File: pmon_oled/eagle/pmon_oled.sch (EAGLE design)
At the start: 37 parts, among them J1 USB, J2 USB, J4 PINHD-1X3, J5 PINHD-2X3, Q1 16Mhz, U1 LTC2943, U2 FT232RL, U3 LT1764AEQ, U4 ATMEGA328TQFP32

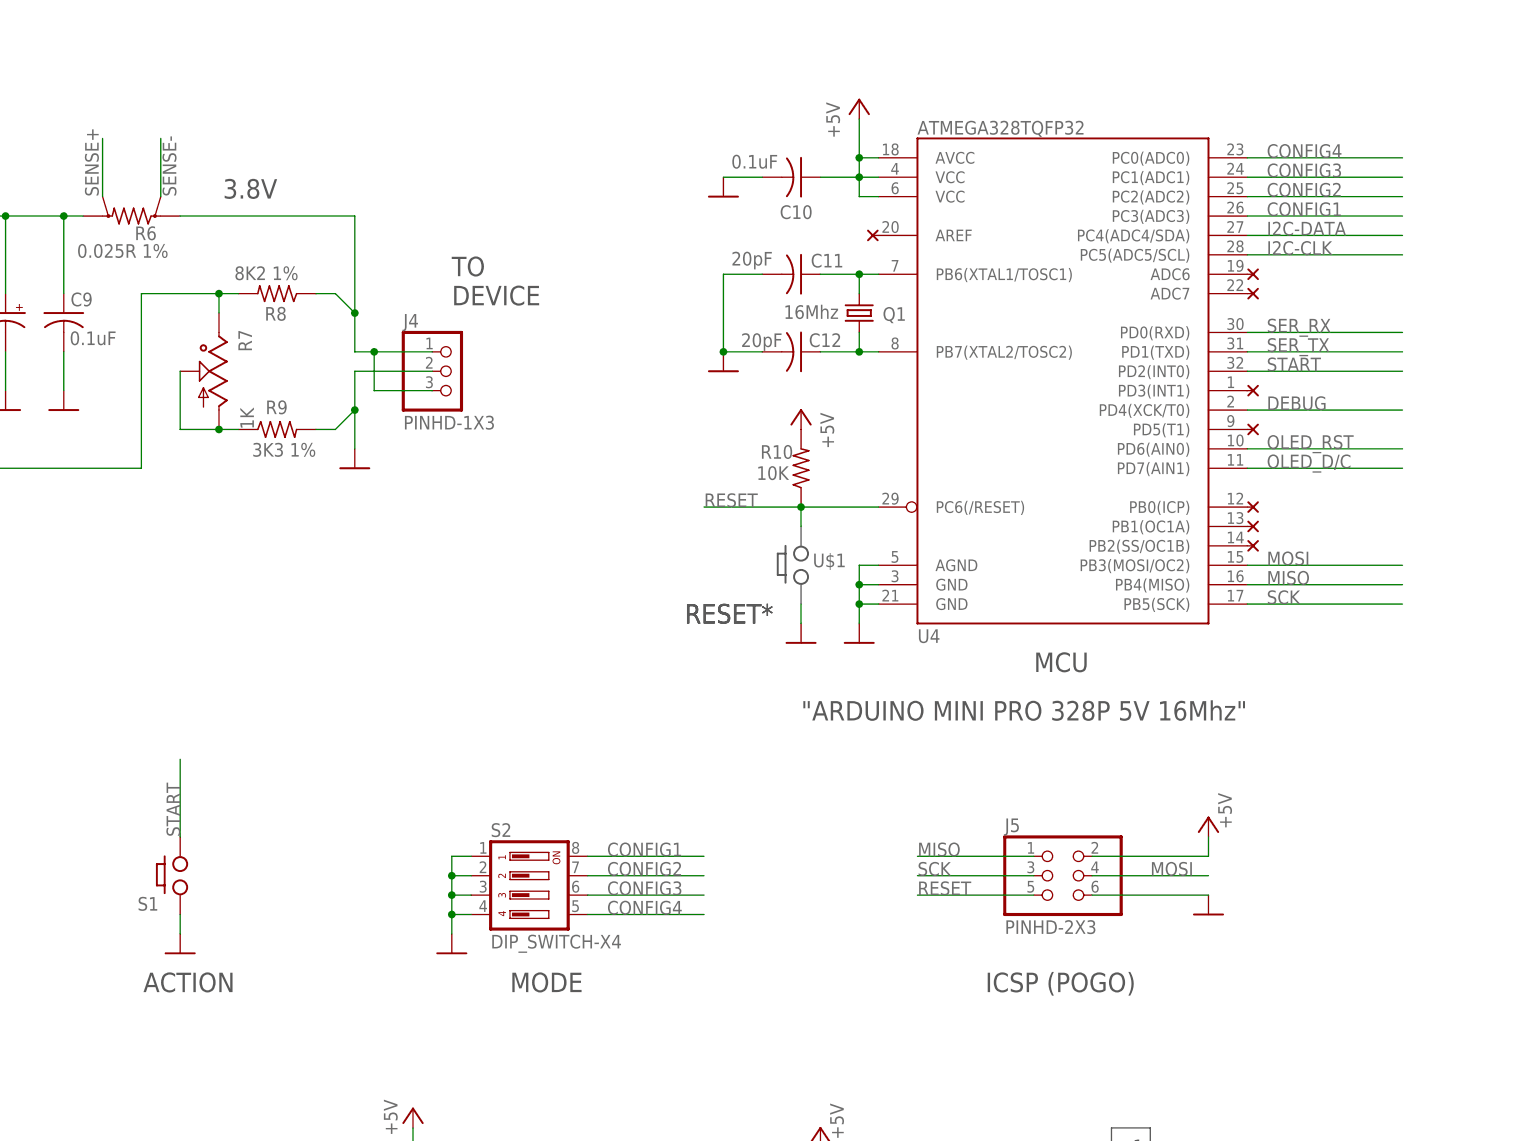
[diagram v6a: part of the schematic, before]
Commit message: Removed the config dip switches.
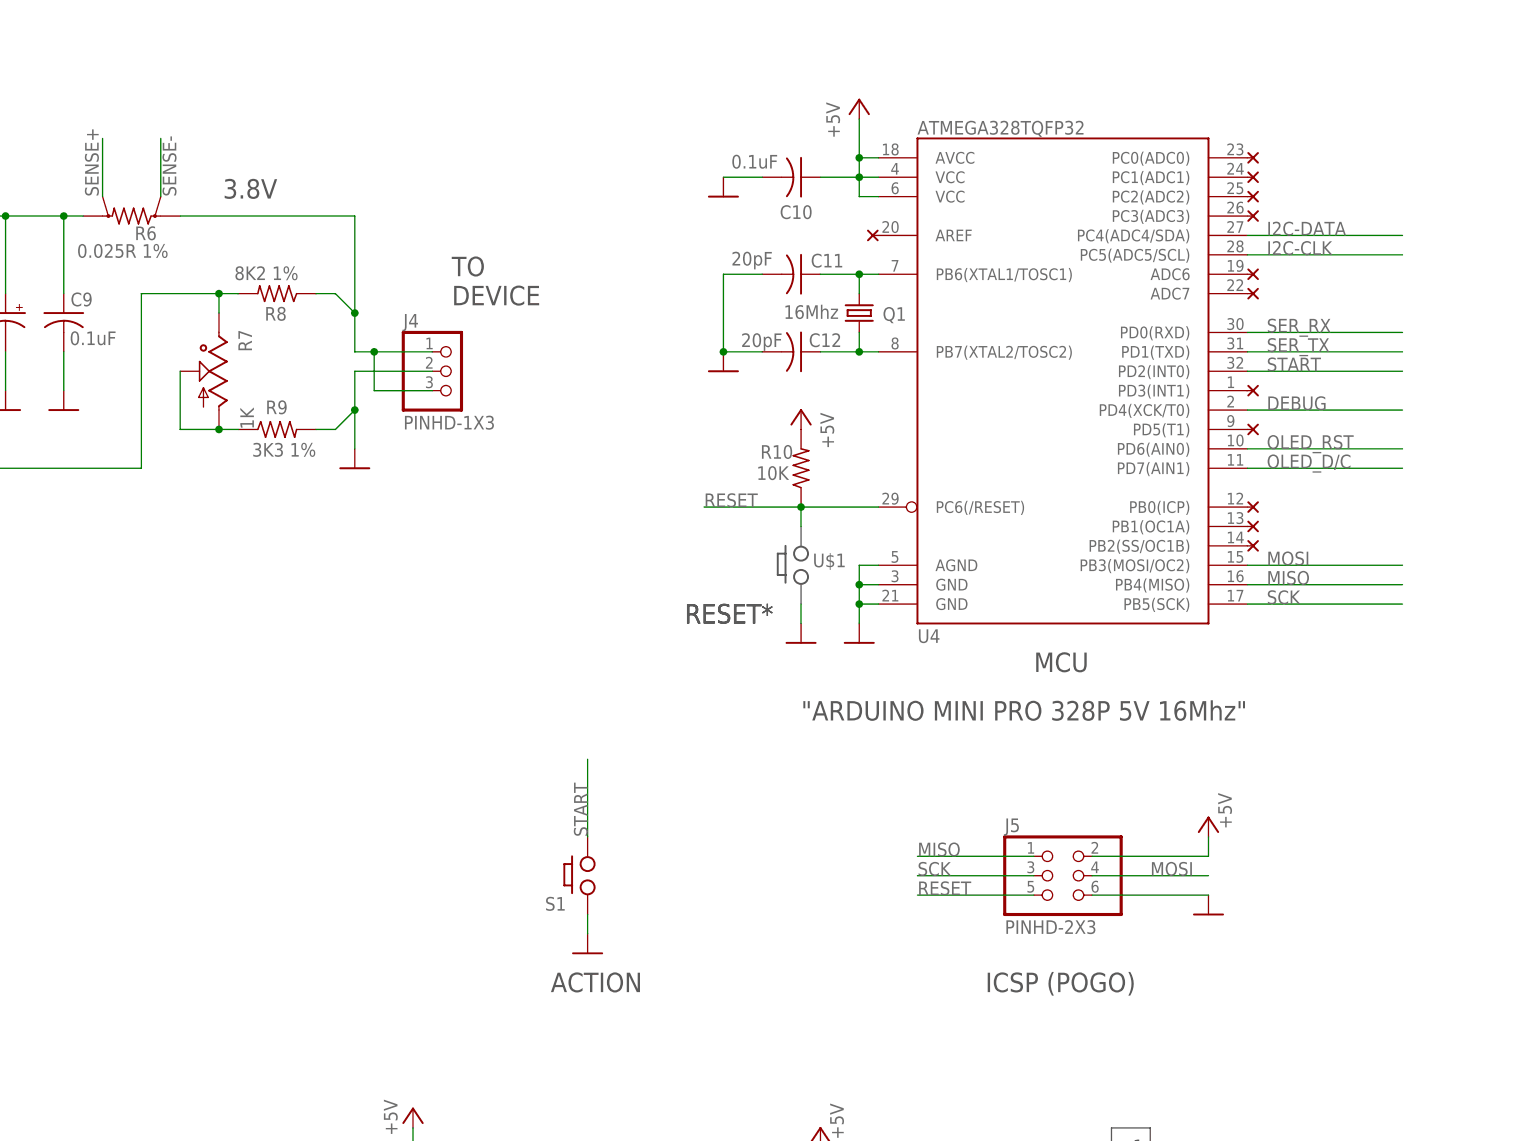
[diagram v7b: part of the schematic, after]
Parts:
- removed S2: DIP_SWITCH-X4, pmon_oled:DIP_SWITCH-X4
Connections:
- removed net CONFIG1: S2.8, U4.PC3(ADC3)
- removed net CONFIG2: S2.7, U4.PC2(ADC2)
- removed net CONFIG3: S2.6, U4.PC1(ADC1)
- removed net CONFIG4: S2.5, U4.PC0(ADC0)
- net GND: no longer S2.1, S2.2, S2.3, S2.4
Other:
- note removed: "MODE"
- moved on the sheet: S1
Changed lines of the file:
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@@
 <part name="P+12" library="pmon_oled" deviceset="+5V" device=""/>
 <part name="GND29" library="pmon_oled" deviceset="GND" device=""/>
-<part name="S2" library="pmon_oled" deviceset="DIP_SWITCH-X4" device=""/>
-<part name="GND30" library="pmon_oled" deviceset="GND" device=""/>
 <part name="J1" library="pmon_oled" deviceset="USB" device=""/>
 <part name="R7" library="pmon_oled" deviceset="TRIM_US-" device="SM-42/43A" value="1K"/>
@@
 <part name="U$14" library="pmon_oled" deviceset="NC" device=""/>
 <part name="S1" library="pmon_oled" deviceset="PUSH_BUTTON" device=""/>
+<part name="U$15" library="pmon_oled" deviceset="NC" device=""/>
+<part name="U$17" library="pmon_oled" deviceset="NC" device=""/>
+<part name="U$18" library="pmon_oled" deviceset="NC" device=""/>
+<part name="U$19" library="pmon_oled" deviceset="NC" device=""/>
 </parts>
 <sheets>
@@
 <text x="134.62" y="194.056" size="2.54" layer="97">TO
 DEVICE</text>
-<text x="142.24" y="104.14" size="2.54" layer="97">MODE</text>
 <text x="104.648" y="208.026" size="2.54" layer="97">3.8V</text>
 <text x="223.774" y="83.058" size="1.778" layer="97">1</text>
@@
 <text x="165.1" y="152.4" size="2.54" layer="97">RESET*</text>
 <text x="180.34" y="139.7" size="2.54" layer="97">"ARDUINO MINI PRO 328P 5V 16Mhz"</text>
-<text x="94.234" y="104.14" size="2.54" layer="97">ACTION</text>
+<text x="147.574" y="104.14" size="2.54" layer="97">ACTION</text>
 <text x="-7.112" y="213.106" size="2.54" layer="97">SOURCE</text>
 <text x="122.936" y="49.784" size="2.54" layer="97">DISPLAY</text>
@@
 </instance>
 <instance part="GND29" gate="1" x="248.92" y="60.96"/>
-<instance part="S2" gate="G$1" x="144.78" y="119.38" rot="R270"/>
-<instance part="GND30" gate="1" x="134.62" y="109.22"/>
 <instance part="J1" gate="G$1" x="-5.08" y="187.96"/>
 <instance part="R7" gate="G$1" x="104.14" y="185.42" smashed="yes" rot="MR0">
@@
 <attribute name="VALUE" x="40.132" y="145.796" size="1.778" layer="96" rot="MR90"/>
 </instance>
-<instance part="GND22" gate="1" x="99.06" y="109.22"/>
+<instance part="GND22" gate="1" x="152.4" y="109.22"/>
 <instance part="J2" gate="G$1" x="-5.08" y="50.8"/>
 <instance part="Q1" gate="G$1" x="187.96" y="193.04" smashed="yes" rot="R270">
@@
 </instance>
 <instance part="U$14" gate="G$1" x="238.76" y="167.64" rot="R180"/>
-<instance part="S1" gate="G$1" x="99.06" y="119.38" smashed="yes">
-<attribute name="NAME" x="93.472" y="114.808" size="1.778" layer="95"/>
-</instance>
+<instance part="S1" gate="G$1" x="152.4" y="119.38" smashed="yes">
+<attribute name="NAME" x="146.812" y="114.808" size="1.778" layer="95"/>
+</instance>
+<instance part="U$15" gate="G$1" x="238.76" y="205.74" rot="R180"/>
+<instance part="U$17" gate="G$1" x="238.76" y="208.28" rot="R180"/>
+<instance part="U$18" gate="G$1" x="238.76" y="210.82" rot="R180"/>
+<instance part="U$19" gate="G$1" x="238.76" y="213.36" rot="R180"/>
 </instances>
 <busses>
@@
 </segment>
 <segment>
-<pinref part="GND30" gate="1" pin="GND"/>
-<wire x1="134.62" y1="111.76" x2="134.62" y2="114.3" width="0.1524" layer="91"/>
-<pinref part="S2" gate="G$1" pin="1"/>
-<wire x1="134.62" y1="114.3" x2="134.62" y2="116.84" width="0.1524" layer="91"/>
-<wire x1="134.62" y1="116.84" x2="134.62" y2="119.38" width="0.1524" layer="91"/>
-<wire x1="134.62" y1="119.38" x2="134.62" y2="121.92" width="0.1524" layer="91"/>
-<wire x1="134.62" y1="121.92" x2="137.16" y2="121.92" width="0.1524" layer="91"/>
-<pinref part="S2" gate="G$1" pin="2"/>
-<wire x1="137.16" y1="119.38" x2="134.62" y2="119.38" width="0.1524" layer="91"/>
-<pinref part="S2" gate="G$1" pin="3"/>
-<wire x1="137.16" y1="116.84" x2="134.62" y2="116.84" width="0.1524" layer="91"/>
-<pinref part="S2" gate="G$1" pin="4"/>
-<wire x1="137.16" y1="114.3" x2="134.62" y2="114.3" width="0.1524" layer="91"/>
-<junction x="134.62" y="119.38"/>
-<junction x="134.62" y="116.84"/>
-<junction x="134.62" y="114.3"/>
-</segment>
-<segment>
 <pinref part="GND17" gate="1" pin="GND"/>
 <pinref part="C1" gate="G$1" pin="2"/>
@@
 <segment>
 <pinref part="GND22" gate="1" pin="GND"/>
-<wire x1="99.06" y1="111.76" x2="99.06" y2="114.3" width="0.1524" layer="91"/>
+<wire x1="152.4" y1="111.76" x2="152.4" y2="114.3" width="0.1524" layer="91"/>
 <pinref part="S1" gate="G$1" pin="1"/>
 </segment>
@@
 </segment>
 </net>
-<net name="CONFIG1" class="0">
-<segment>
-<pinref part="S2" gate="G$1" pin="8"/>
-<wire x1="152.4" y1="121.92" x2="167.64" y2="121.92" width="0.1524" layer="91"/>
-<label x="154.94" y="121.92" size="1.778" layer="95"/>
-</segment>
-<segment>
-<wire x1="238.76" y1="205.74" x2="259.08" y2="205.74" width="0.1524" layer="91"/>
-<label x="241.3" y="205.74" size="1.778" layer="95"/>
-<pinref part="U4" gate="G$1" pin="PC3(ADC3)"/>
-</segment>
-</net>
-<net name="CONFIG2" class="0">
-<segment>
-<pinref part="S2" gate="G$1" pin="7"/>
-<wire x1="152.4" y1="119.38" x2="167.64" y2="119.38" width="0.1524" layer="91"/>
-<label x="154.94" y="119.38" size="1.778" layer="95"/>
-</segment>
-<segment>
-<wire x1="238.76" y1="208.28" x2="259.08" y2="208.28" width="0.1524" layer="91"/>
-<label x="241.3" y="208.28" size="1.778" layer="95"/>
-<pinref part="U4" gate="G$1" pin="PC2(ADC2)"/>
-</segment>
-</net>
-<net name="CONFIG3" class="0">
-<segment>
-<pinref part="S2" gate="G$1" pin="6"/>
-<wire x1="152.4" y1="116.84" x2="167.64" y2="116.84" width="0.1524" layer="91"/>
-<label x="154.94" y="116.84" size="1.778" layer="95"/>
-</segment>
-<segment>
-<wire x1="238.76" y1="210.82" x2="259.08" y2="210.82" width="0.1524" layer="91"/>
-<label x="241.3" y="210.82" size="1.778" layer="95"/>
-<pinref part="U4" gate="G$1" pin="PC1(ADC1)"/>
-</segment>
-</net>
-<net name="CONFIG4" class="0">
-<segment>
-<pinref part="S2" gate="G$1" pin="5"/>
-<wire x1="152.4" y1="114.3" x2="167.64" y2="114.3" width="0.1524" layer="91"/>
-<label x="154.94" y="114.3" size="1.778" layer="95"/>
-</segment>
-<segment>
-<wire x1="238.76" y1="213.36" x2="259.08" y2="213.36" width="0.1524" layer="91"/>
-<label x="241.3" y="213.36" size="1.778" layer="95"/>
-<pinref part="U4" gate="G$1" pin="PC0(ADC0)"/>
-</segment>
-</net>
 <net name="N$18" class="0">
 <segment>
@@
 </segment>
 <segment>
-<wire x1="99.06" y1="124.46" x2="99.06" y2="134.62" width="0.1524" layer="91"/>
-<label x="99.06" y="124.46" size="1.778" layer="95" rot="R90"/>
+<wire x1="152.4" y1="124.46" x2="152.4" y2="134.62" width="0.1524" layer="91"/>
+<label x="152.4" y="124.46" size="1.778" layer="95" rot="R90"/>
 <pinref part="S1" gate="G$1" pin="2"/>
 </segment>
